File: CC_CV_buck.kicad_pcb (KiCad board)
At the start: 4 copper layers, 103 x 43 mm, 61 parts, among them Q1 TIP42C, Q2 AO3400A, Q3 MMBT3906, Q4 MMBT3904, U1 OPA2197xD, U2 INA194, U3 AOZ6605PI-1

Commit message: clean pcb a little
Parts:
- moved RV3 68.3 mm to (68.8, 103.0)
- moved RV1 58.2 mm to (89.5, 102.8)
- moved RV2 58.2 mm to (112.6, 102.8)
- moved R2 41.9 mm to (64.6, 140.2)
- moved R16 38.6 mm to (59.6, 146.6)
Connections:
- RV1 pad 1: unconnected-(RV1-Pad1) -> Vcc
- RV1 pad 2: unconnected-(RV1-Pad2) -> /VSET
- RV1 pad 3: unconnected-(RV1-Pad3) -> GND
- RV2 pad 1: unconnected-(RV2-Pad1) -> Vcc
- RV2 pad 2: unconnected-(RV2-Pad2) -> /ISET
- RV2 pad 3: unconnected-(RV2-Pad3) -> GND
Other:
- board text removed: "test"
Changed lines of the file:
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@@
 	(net 33 "/BUCK_FB")
 	(net 34 "Net-(R16-Pad2)")
-	(net 35 "unconnected-(RV1-Pad3)")
-	(net 36 "unconnected-(RV1-Pad2)")
-	(net 37 "unconnected-(RV1-Pad1)")
-	(net 38 "unconnected-(RV2-Pad1)")
-	(net 39 "unconnected-(RV2-Pad3)")
-	(net 40 "unconnected-(RV2-Pad2)")
 	(footprint "10uH_inductor:L_Abracon_ASPI-1040HI"
 		(layer "F.Cu")
@@
 	(footprint "potentiometer:POT_PTN16-A20120K1B1"
 		(layer "F.Cu")
-		(at 111.952 155.99)
+		(at 68.8 103)
 		(property "Reference" "RV3"
 			(at -0.575 -8.675 0)
@@
 	(footprint "potentiometer:POT_PTN16-A20120K1B1"
 		(layer "F.Cu")
-		(at 88.8885 155.99)
+		(at 112.6 102.8)
 		(property "Reference" "RV2"
 			(at -0.575 -8.675 0)
@@
 			(layers "*.Cu" "*.Mask")
 			(remove_unused_layers no)
-			(net 38 "unconnected-(RV2-Pad1)")
+			(net 9 "Vcc")
 			(pinfunction "1")
 			(pintype "passive")
@@
 			(layers "*.Cu" "*.Mask")
 			(remove_unused_layers no)
-			(net 40 "unconnected-(RV2-Pad2)")
+			(net 24 "/ISET")
 			(pinfunction "2")
 			(pintype "passive")
@@
 			(layers "*.Cu" "*.Mask")
 			(remove_unused_layers no)
-			(net 39 "unconnected-(RV2-Pad3)")
+			(net 6 "GND")
 			(pinfunction "3")
 			(pintype "passive")
@@
 	(footprint "potentiometer:POT_PTN16-A20120K1B1"
 		(layer "F.Cu")
-		(at 65.825 155.99)
+		(at 89.5365 102.8)
 		(property "Reference" "RV1"
 			(at -0.575 -8.675 0)
@@
 			(layers "*.Cu" "*.Mask")
 			(remove_unused_layers no)
-			(net 37 "unconnected-(RV1-Pad1)")
+			(net 9 "Vcc")
 			(pinfunction "1")
 			(pintype "passive")
@@
 			(layers "*.Cu" "*.Mask")
 			(remove_unused_layers no)
-			(net 36 "unconnected-(RV1-Pad2)")
+			(net 25 "/VSET")
 			(pinfunction "2")
 			(pintype "passive")
@@
 			(layers "*.Cu" "*.Mask")
 			(remove_unused_layers no)
-			(net 35 "unconnected-(RV1-Pad3)")
+			(net 6 "GND")
 			(pinfunction "3")
 			(pintype "passive")
@@
 	(footprint "Resistor_SMD:R_0805_2012Metric_Pad1.20x1.40mm_HandSolder"
 		(layer "F.Cu")
-		(at 63.4 182.05)
+		(at 64.6 140.2)
 		(descr "Resistor SMD 0805 (2012 Metric), square (rectangular) end terminal, IPC_7351 nominal with elongated pad for handsoldering. (Body size source: IPC-SM-782 page 72, https://www.pcb-3d.com/wordpress/wp-content/uploads/ipc-sm-782a_amendment_1_and_2.pdf), generated with kicad-footprint-generator")
 		(tags "resistor handsolder")
@@
 	(footprint "Resistor_SMD:R_0805_2012Metric_Pad1.20x1.40mm_HandSolder"
 		(layer "F.Cu")
-		(at 63.4 185)
+		(at 59.6 146.6)
 		(descr "Resistor SMD 0805 (2012 Metric), square (rectangular) end terminal, IPC_7351 nominal with elongated pad for handsoldering. (Body size source: IPC-SM-782 page 72, https://www.pcb-3d.com/wordpress/wp-content/uploads/ipc-sm-782a_amendment_1_and_2.pdf), generated with kicad-footprint-generator")
 		(tags "resistor handsolder")
@@
 		(layer "Edge.Cuts")
 	)
-	(gr_text "test"
-		(at 85.2 101.6 0)
-		(layer "F.SilkS")
-		(effects
-			(font
-				(size 1.5 1.5)
-				(thickness 0.3)
-				(bold yes)
-			)
-			(justify left bottom)
-		)
-	)
 	(segment

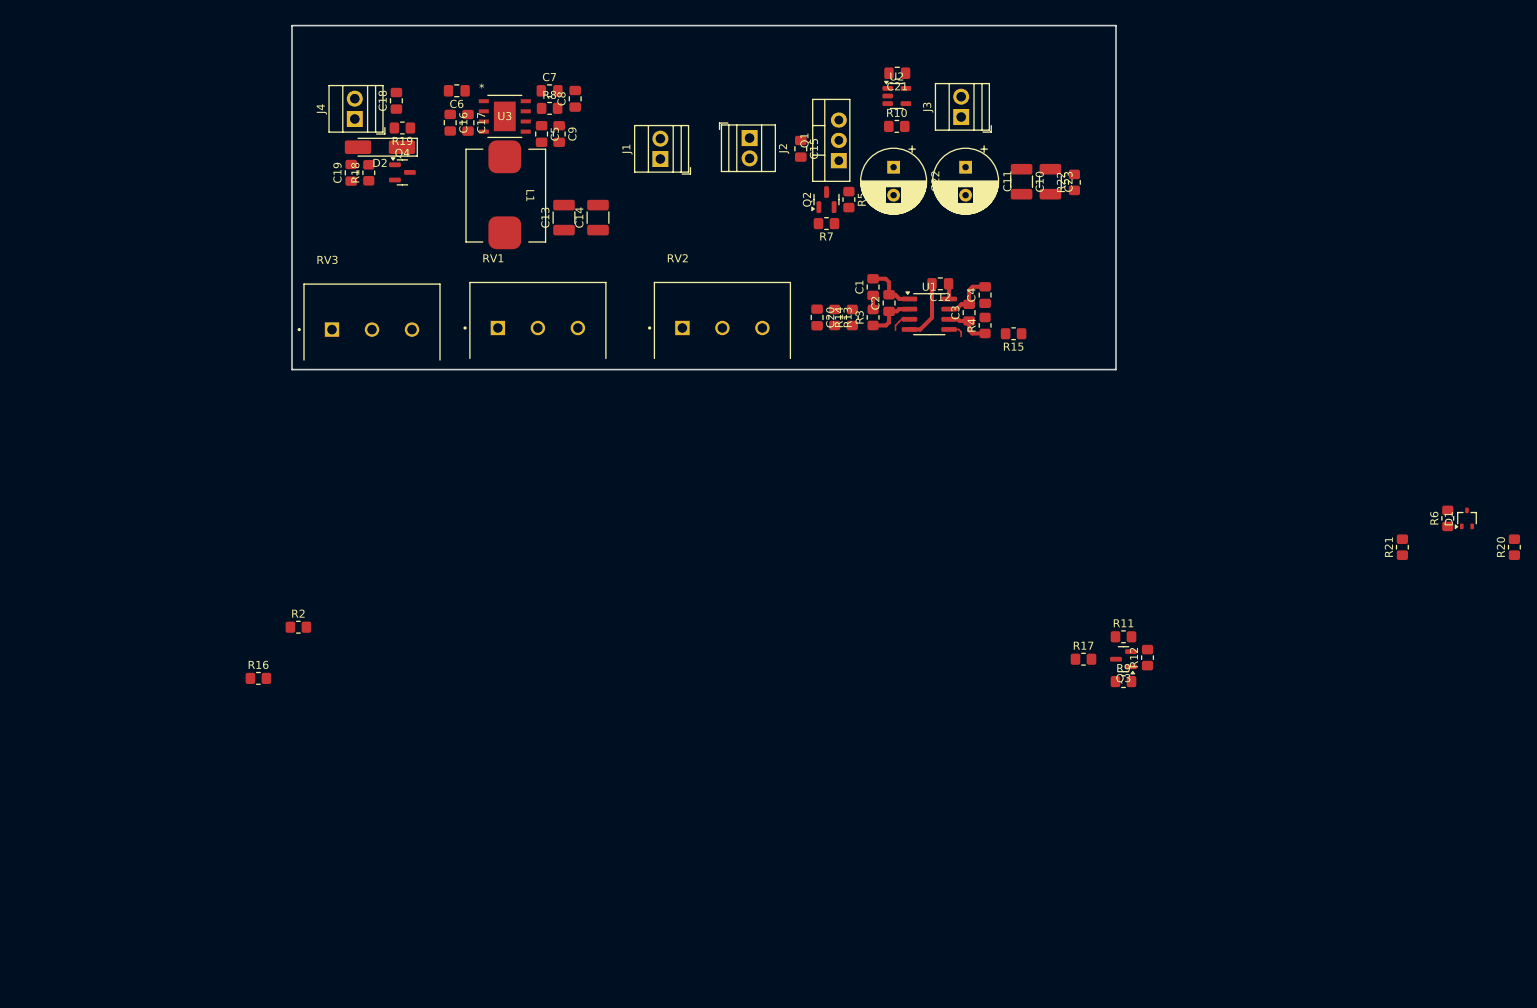
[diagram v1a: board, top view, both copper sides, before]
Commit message: sorta finalize component placement as well as schematic
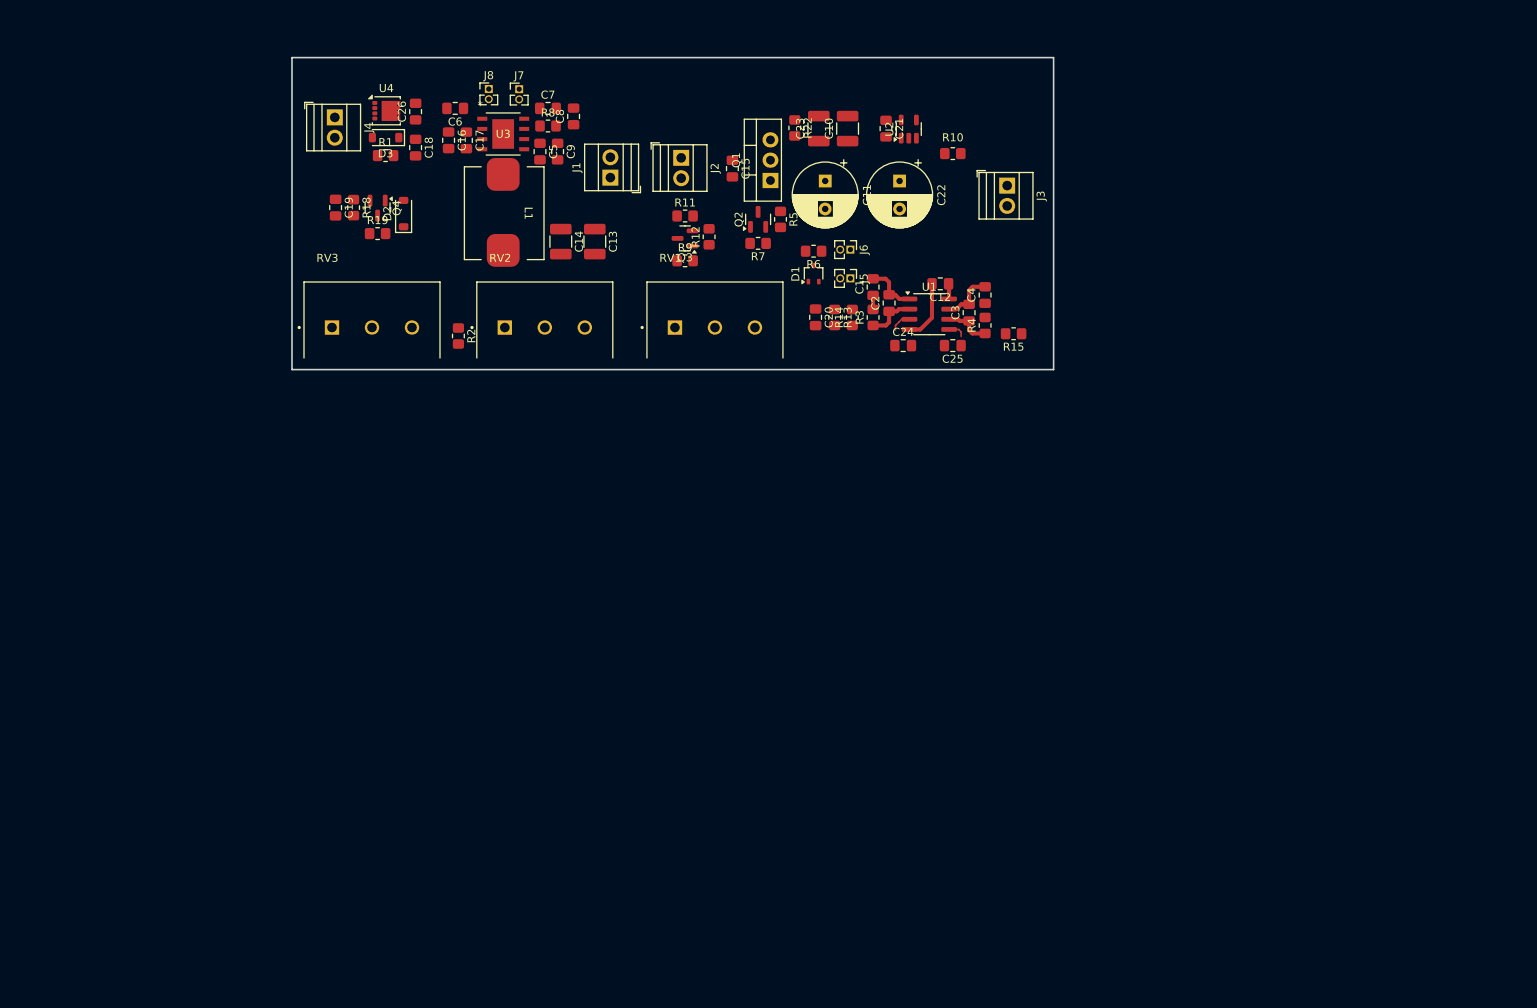
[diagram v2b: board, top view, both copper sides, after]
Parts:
- removed R16, R17, R20, R21: 0, Resistor_SMD:R_0805_2012Metric_Pad1.20x1.40mm_HandSolder
- added C24: 1u, Capacitor_SMD:C_0805_2012Metric_Pad1.18x1.45mm_HandSolder, F.Cu at (140.2, 105.0)
- added C25: 1u, Capacitor_SMD:C_0805_2012Metric_Pad1.18x1.45mm_HandSolder, F.Cu at (146.4, 105.0)
- added C26: 4u7, Capacitor_SMD:C_0805_2012Metric_Pad1.18x1.45mm_HandSolder, F.Cu at (79.2, 75.8)
- added D3: MMSZ5240BT1G, Diode_SMD:D_SOD-123, F.Cu at (75.5, 79.0)
- added J5: Conn_01x02_Pin, Connector_PinHeader_1.27mm:PinHeader_1x02_P1.27mm_Vertical, F.Cu at (133.6, 96.6)
- added J6: Conn_01x02_Pin, Connector_PinHeader_1.27mm:PinHeader_1x02_P1.27mm_Vertical, F.Cu at (133.6, 93.0)
- added J7: Conn_01x02_Pin, Connector_PinHeader_1.27mm:PinHeader_1x02_P1.27mm_Vertical, F.Cu at (92.2, 73.0)
- added J8: Conn_01x02_Pin, Connector_PinHeader_1.27mm:PinHeader_1x02_P1.27mm_Vertical, F.Cu at (88.4, 72.9)
- added R1: 10k, Resistor_SMD:R_0805_2012Metric_Pad1.20x1.40mm_HandSolder, F.Cu at (75.5, 81.2)
- added U4: CSD25402Q3A, Package_SON:VSON-8_3.3x3.3mm_P0.65mm_NexFET, F.Cu at (75.6, 75.6)
- C18: value tbd -> 4u7
- D2: value ZMMxx -> MMSZ5240BT1G; footprint Diode_SMD:D_MiniMELF_Handsoldering -> Diode_SMD:D_SOD-123
- moved D1 87.2 mm to (129.0, 96.0)
- moved R6 86.0 mm to (129.0, 93.2), turned to 180 degrees
- moved R11 76.0 mm to (112.9, 88.8)
- moved Q3 76.0 mm to (112.9, 91.6)
- moved R12 76.0 mm to (115.9, 91.4)
- moved R9 76.0 mm to (112.9, 94.4)
- moved R2 41.5 mm to (84.6, 103.8), turned to -90 degrees
- moved R22 35.6 mm to (126.7, 77.8), turned to -90 degrees
- moved C23 29.7 mm to (129.7, 77.9), turned to 90 degrees
- moved C10 22.7 mm to (133.2, 77.9), turned to 90 degrees
- moved RV2 22.2 mm to (90.4, 102.7)
- moved RV1 22.1 mm to (111.7, 102.7)
- moved C11 17.6 mm to (130.4, 84.4)
- moved R19 13.6 mm to (74.5, 91.0), turned to 0 degrees
- moved J3 10.3 mm to (153.2, 85.0), turned to -90 degrees
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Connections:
- J4 pad 1: P13V0 -> VIN
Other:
- board size 103 x 43 mm -> 95.2 x 39 mm

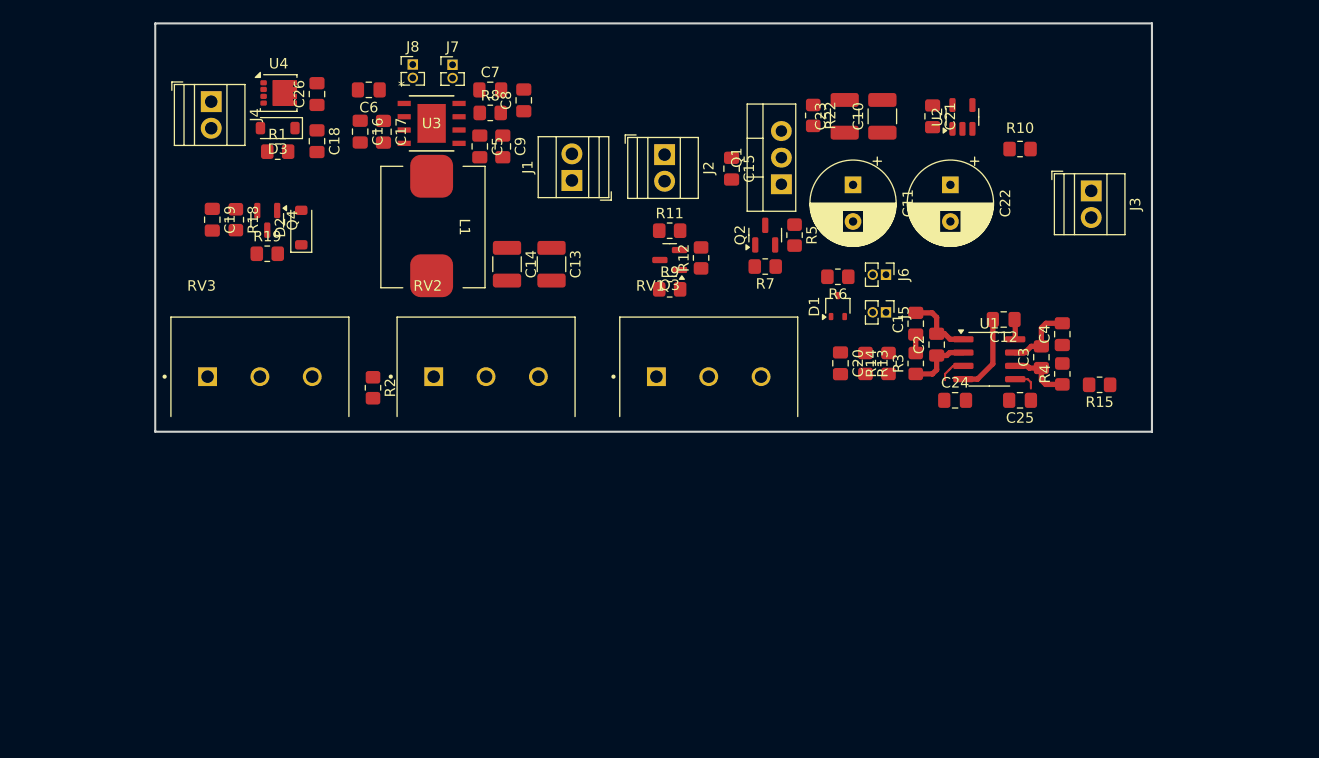
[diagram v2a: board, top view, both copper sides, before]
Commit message: add comp values for LDO, mess with layout a bit to see MH placement
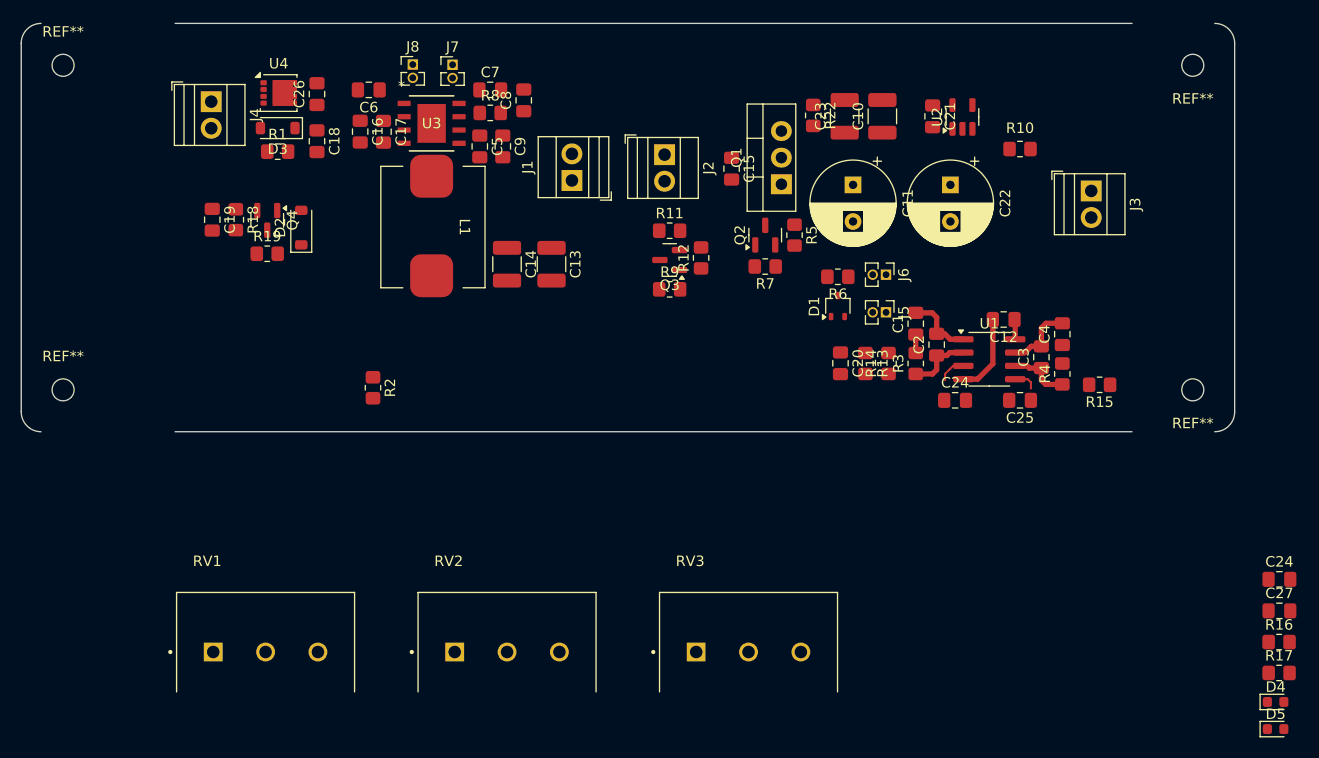
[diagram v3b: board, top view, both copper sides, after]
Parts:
- added C24: 1u, Capacitor_SMD:C_0805_2012Metric_Pad1.18x1.45mm_HandSolder, F.Cu at (171.2, 122.1)
- added C27: tbd, Capacitor_SMD:C_0805_2012Metric_Pad1.18x1.45mm_HandSolder, F.Cu at (171.2, 125.1)
- added D4: LED, LED_SMD:LED_0603_1608Metric, F.Cu at (170.8, 133.8)
- added D5: LED, LED_SMD:LED_0603_1608Metric, F.Cu at (170.8, 136.4)
- added R16: 10k, Resistor_SMD:R_0805_2012Metric_Pad1.20x1.40mm_HandSolder, F.Cu at (171.1, 128.1)
- added R17: 10k, Resistor_SMD:R_0805_2012Metric_Pad1.20x1.40mm_HandSolder, F.Cu at (171.1, 131.0)
- added REF**: MountingHole_2.1mm, MountingHole:MountingHole_2.1mm, F.Cu at (162.9, 73.0)
- added REF**: MountingHole_2.1mm, MountingHole:MountingHole_2.1mm, F.Cu at (162.9, 104.0)
- added REF**: MountingHole_2.1mm, MountingHole:MountingHole_2.1mm, F.Cu at (55.0, 73.0)
- added REF**: MountingHole_2.1mm, MountingHole:MountingHole_2.1mm, F.Cu at (55.0, 104.0)
- RV1, RV2: value tbd -> 20k
- moved RV3 53.6 mm to (115.5, 129.0)
- moved RV1 49.8 mm to (69.3, 129.0)
- moved RV2 26.4 mm to (92.4, 129.0)
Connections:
- net Net-(J5-Pin_1) renamed /CV_out
- net Net-(J6-Pin_1) renamed /CC_out
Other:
- board size 95.2 x 39 mm -> 115.9 x 39 mm

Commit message: more or less done w/ schematic and component placement
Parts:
- removed the C24 at (140.2, 105.0)
- removed the C24 at (171.2, 122.1)
- removed REF** (x4): MountingHole_2.1mm, MountingHole:MountingHole_2.1mm
- added C24: 1u, Capacitor_SMD:C_0805_2012Metric_Pad1.18x1.45mm_HandSolder, F.Cu at (141.9, 104.3)
- added H1: MountingHole_Pad, MountingHole:MountingHole_2.2mm_M2_ISO7380_Pad, F.Cu at (54.9, 72.9)
- added H2: MountingHole_Pad, MountingHole:MountingHole_2.2mm_M2_ISO7380_Pad, F.Cu at (163.0, 72.9)
- added H3: MountingHole_Pad, MountingHole:MountingHole_2.2mm_M2_ISO7380_Pad, F.Cu at (163.0, 104.1)
- added H4: MountingHole_Pad, MountingHole:MountingHole_2.2mm_M2_ISO7380_Pad, F.Cu at (54.9, 104.1)
- C1: value tbd -> 4n7
- C10, C13, C23: value tbd -> 15u
- C11, C22: value tbd -> 220u
- C14: value tbd -> 220u; footprint Capacitor_SMD:C_1210_3225Metric_Pad1.33x2.70mm_HandSolder -> Capacitor_THT:CP_Radial_D8.0mm_P3.50mm
- C15: value tbd -> 15u; footprint Capacitor_SMD:C_0805_2012Metric_Pad1.18x1.45mm_HandSolder -> Capacitor_SMD:C_1210_3225Metric_Pad1.33x2.70mm_HandSolder
- C16, C17: value 4u7 -> 15u; footprint Capacitor_SMD:C_0805_2012Metric_Pad1.18x1.45mm_HandSolder -> Capacitor_SMD:C_1210_3225Metric_Pad1.33x2.70mm_HandSolder
- C2: value tbd -> 4p7
- C4: value tbd -> 1n
- J1, J2, J3, J4: footprint TerminalBlock:TerminalBlock_Xinya_XY308-2.54-2P_1x02_P2.54mm_Horizontal -> TerminalBlock_Phoenix:TerminalBlock_Phoenix_MPT-0,5-2-2.54_1x02_P2.54mm_Horizontal
- R13, R14, R15: value tbd -> 5k
- R3: value tbd -> 50k
- R4: value tbd -> 100k
- moved D4 78.1 mm to (106.5, 89.5), turned to 90 degrees
- moved D5 76.4 mm to (110.5, 89.5), turned to 90 degrees
- moved R16 73.4 mm to (106.5, 93.3), turned to -90 degrees
- moved R17 71.4 mm to (110.5, 93.3), turned to -90 degrees
- moved RV3 57.2 mm to (64.0, 104.0)
- moved RV1 46.1 mm to (108.0, 104.0)
- moved C27 29.2 mm to (155.8, 100.3)
- moved RV2 25.8 mm to (86.3, 103.9)
- moved C15 24.4 mm to (141.6, 74.0)
- moved R22 20.0 mm to (145.6, 84.2), turned to 90 degrees
- moved R7 18.8 mm to (124.2, 73.6), turned to 90 degrees
- moved Q2 16.5 mm to (127.2, 73.6), turned to 0 degrees
- moved J4 16.1 mm to (56.0, 85.8)
- moved C23 14.4 mm to (142.6, 84.2), turned to -90 degrees
- moved C21 13.7 mm to (151.6, 76.2), turned to 180 degrees
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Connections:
- J3 pad 1: VOUT_LDO -> GND
- J3 pad 2: GND -> VOUT_LDO
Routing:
- net /ISET: track 2.22 -> 64.5 mm
- net /VSET: track 2.67 -> 34.4 mm
- net /CC_out: track 6.69 -> 28.1 mm
- net /SW: track 0.00 -> 11.0 mm
- net Net-(J8-Pin_1): track 0.00 -> 11.0 mm
- net /V_SNS: track 6.19 -> 13.4 mm
- net VOUT_LDO: track 0.00 -> 6.67 mm
- net /BUCK_VCC: track 0.00 -> 5.70 mm
- net Net-(U1B--): track 5.91 -> 11.0 mm
- net Net-(Q1-C): track 0.00 -> 4.26 mm
- net /CV_out: track 6.57 -> 10.7 mm
- net /I_SNS: track 0.00 -> 2.53 mm
- net /BST: track 0.00 -> 2.37 mm
- net /BUCK_COMP: track 0.00 -> 2.33 mm
- net Net-(C4-Pad1): track 0.00 -> 1.76 mm
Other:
- board text added: "CC"
- board text added: "CV"
